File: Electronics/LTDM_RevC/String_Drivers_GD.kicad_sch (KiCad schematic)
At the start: 25 parts, among them Q1 FQP27P06, Q2 IRLZ44N, Q3 FQP27P06, Q4 IRLZ44N, U11 LM7332, U12 TC4427xOA, U9 TC4426

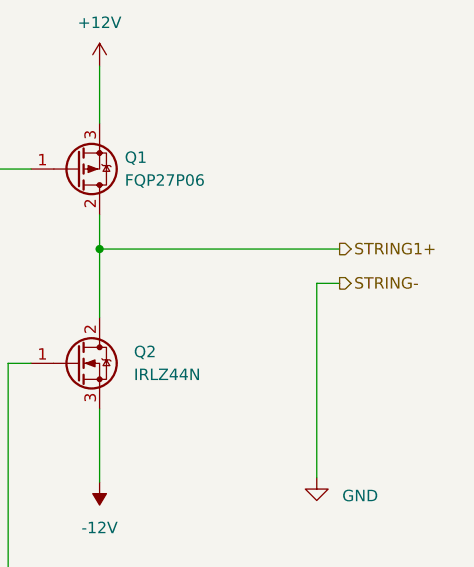
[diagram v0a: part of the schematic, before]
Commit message: Improved  and characterized ADC sample time
Previously took ~6.3uS to sample both ADCs but have gotten it down to a sweet ~3.4uS by disabling 'long sampling mode' and ADC_CFG_ADSTS(3) to ADC_CFG_ADSTS(0). Apparently that was upping sample time.

This arrangement is likely noisier but gives a user an extra 3.5uS to play with in render()

This is for 600MHz.

Trimming away old code too :)
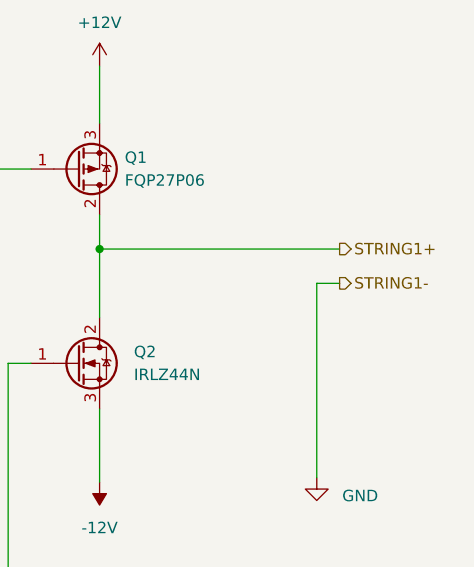
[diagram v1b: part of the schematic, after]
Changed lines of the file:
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@@
 		)
 	)
-	(hierarchical_label "STRING-"
+	(hierarchical_label "STRING1-"
 		(shape output)
 		(at 209.55 54.61 0)
